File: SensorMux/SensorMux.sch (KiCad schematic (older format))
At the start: 0 parts

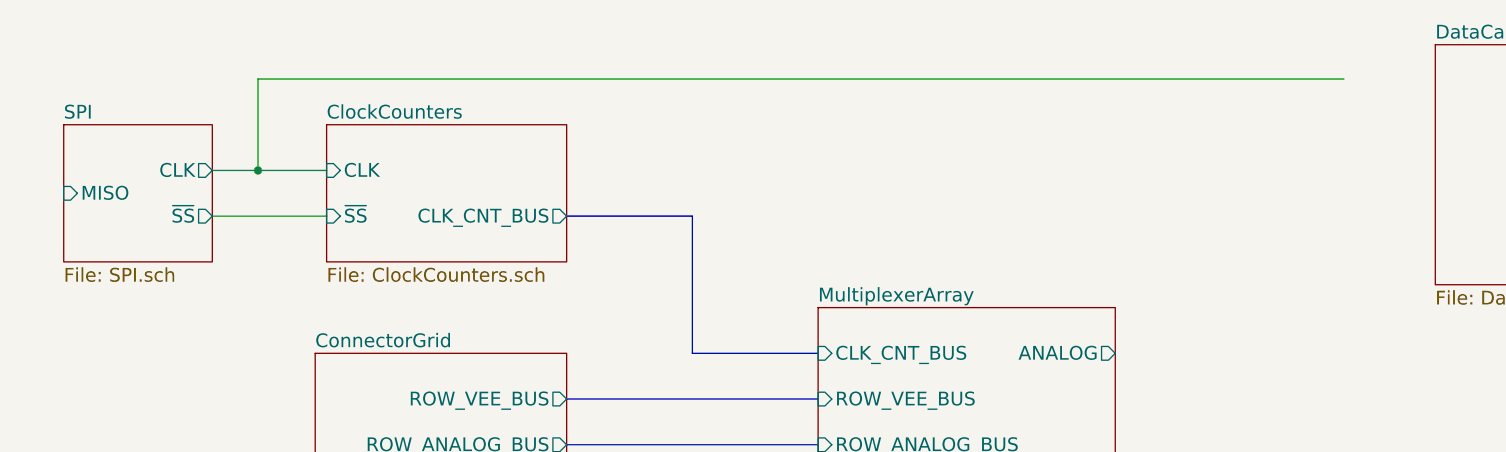
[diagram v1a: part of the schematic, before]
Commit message: Working on adding analog part with SPI adjustment so the computer can control the opamps without needing manual trimpots.
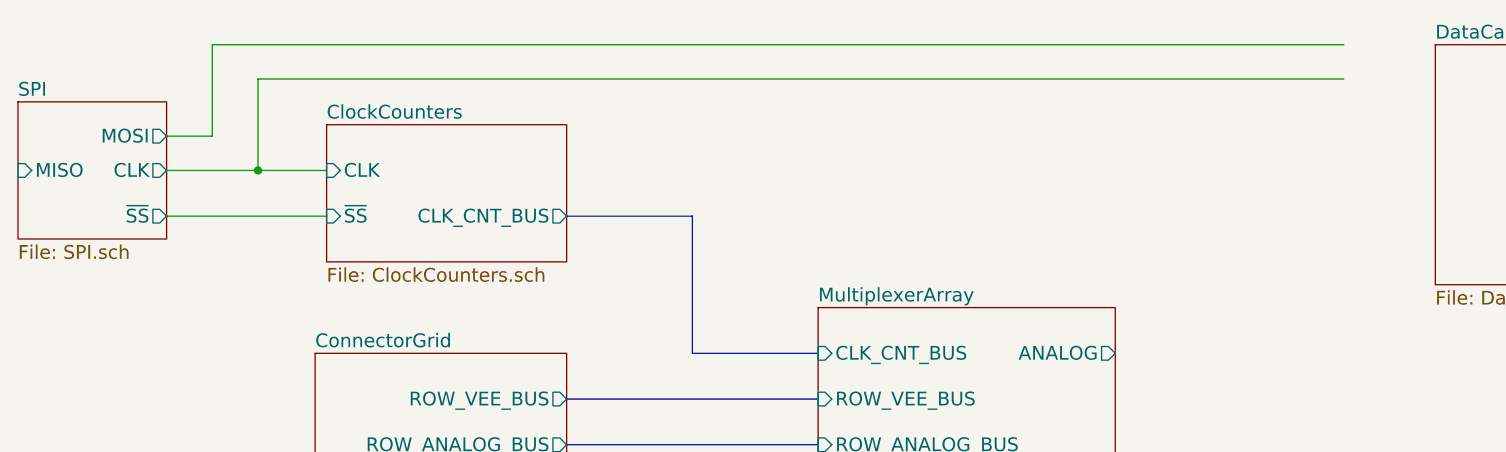
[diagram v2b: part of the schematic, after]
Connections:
- wire segments 4 -> 7
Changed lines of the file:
@@
 $EndSheet
 $Sheet
-S 1150 3500 650  600
+S 950  3400 650  600
 U 5A4A9682
 F0 "SPI" 60
 F1 "SPI.sch" 60
-F2 "MISO" I L 1150 3800 60
-F3 "~SS" O R 1800 3900 60
-F4 "CLK" O R 1800 3700 60
+F2 "MISO" I L 950 3700 60
+F3 "~SS" O R 1600 3900 60
+F4 "CLK" O R 1600 3700 60
+F5 "MOSI" O R 1600 3550 60
 $EndSheet
 $Sheet
@@
 $EndSheet
 Wire Wire Line
-	1800 3700 2300 3700
+	1600 3700 2300 3700
 Wire Wire Line
-	1800 3900 2300 3900
+	1600 3900 2300 3900
 Wire Bus Line
 	3350 3900 3900 3900
@@
 	2000 3300 6750 3300
 Connection ~ 2000 3700
+Wire Wire Line
+	1600 3550 1800 3550
+Wire Wire Line
+	1800 3550 1800 3150
+Wire Wire Line
+	1800 3150 6750 3150
 $EndSCHEMATC

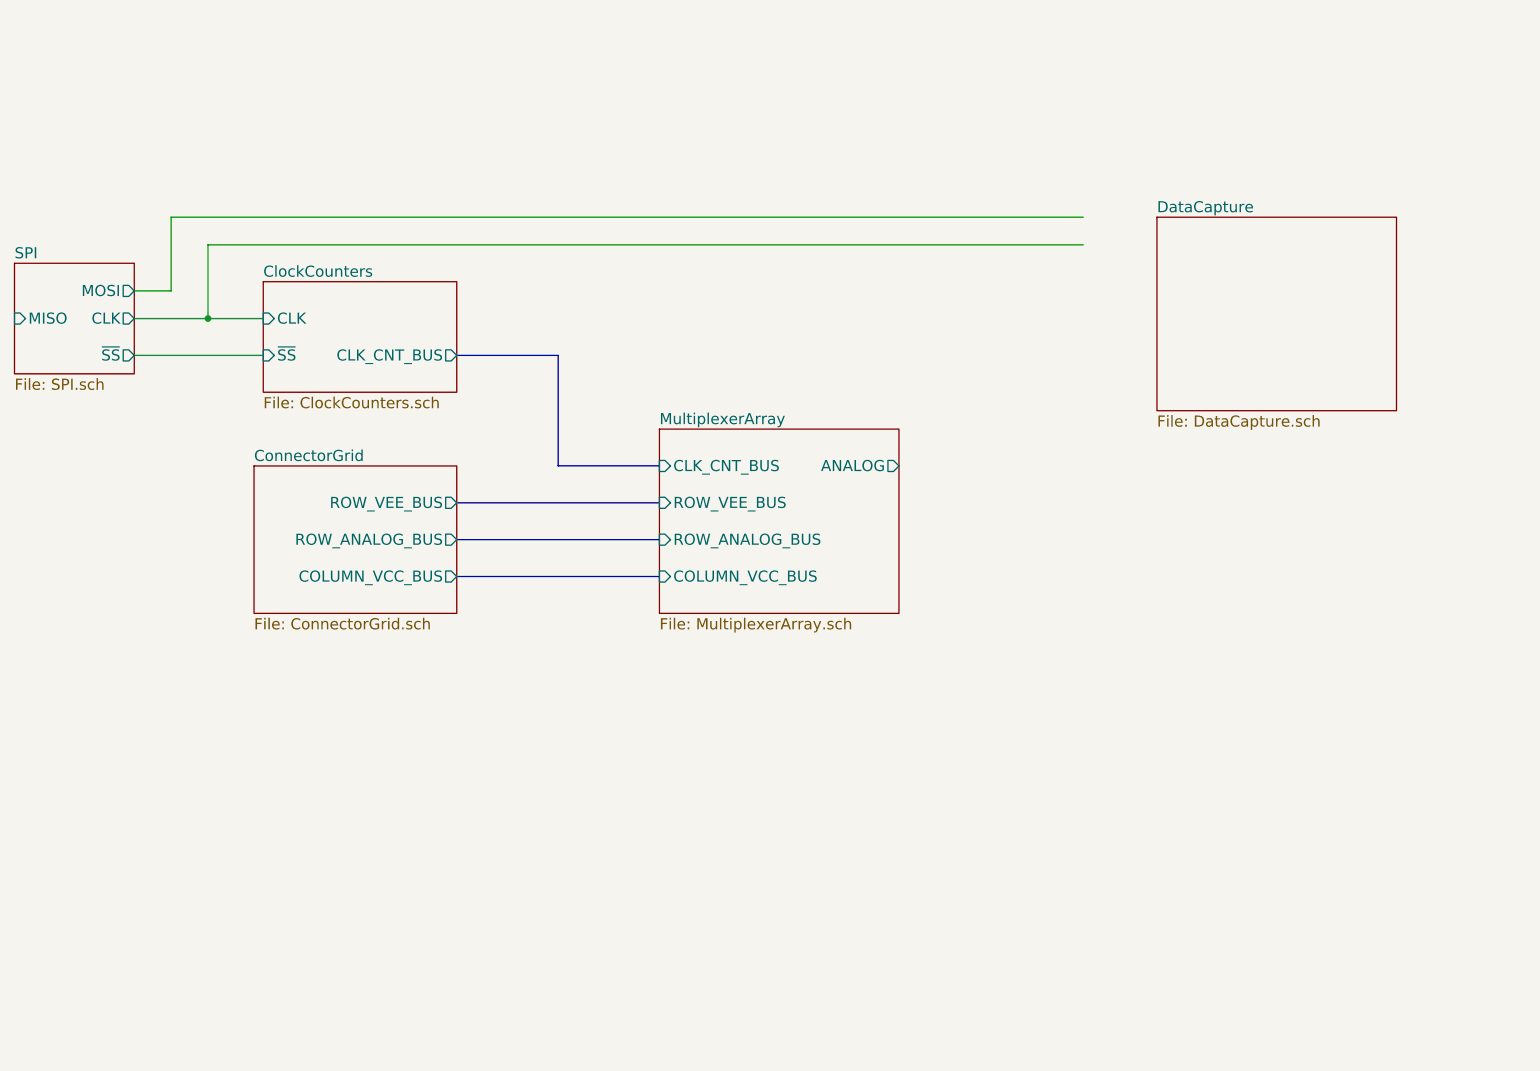
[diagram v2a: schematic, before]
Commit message: Working on the analog input.
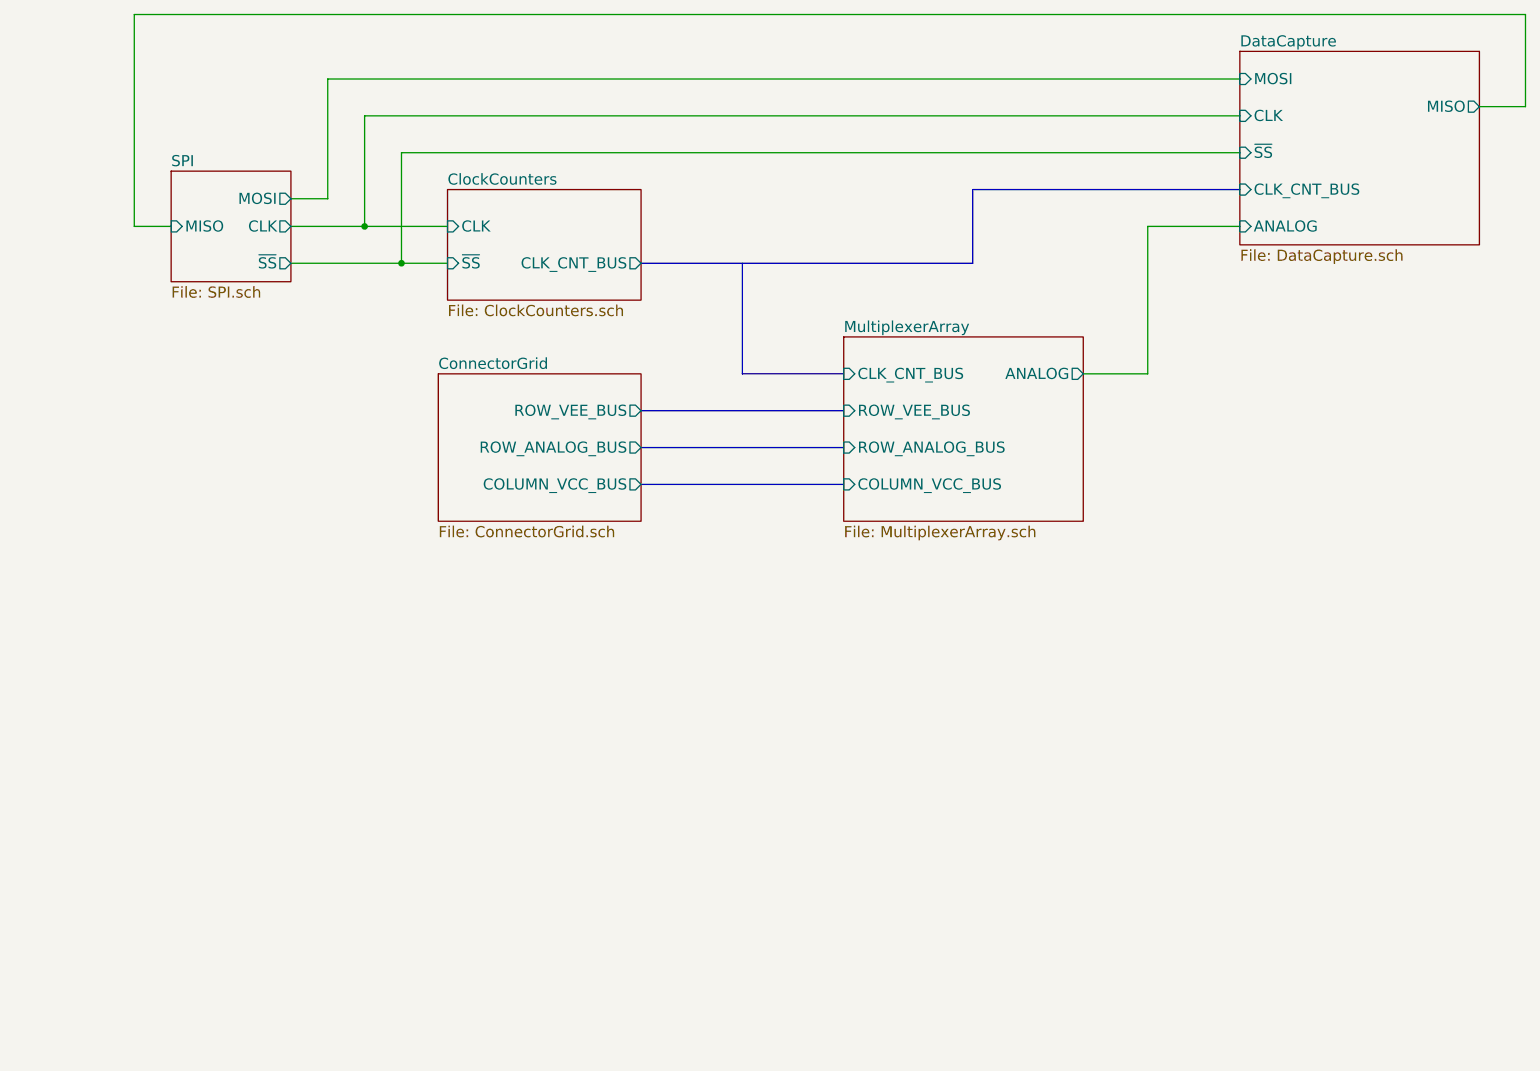
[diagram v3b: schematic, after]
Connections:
- wire segments 7 -> 17
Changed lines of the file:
@@
 $EndDescr
 $Sheet
-S 2300 3500 1050 600
+S 3300 3000 1050 600
 U 5A4A7F2E
 F0 "ClockCounters" 60
 F1 "ClockCounters.sch" 60
-F2 "~SS" I L 2300 3900 60
-F3 "CLK" I L 2300 3700 60
-F4 "CLK_CNT_BUS" O R 3350 3900 60
+F2 "~SS" I L 3300 3400 60
+F3 "CLK" I L 3300 3200 60
+F4 "CLK_CNT_BUS" O R 4350 3400 60
 $EndSheet
 $Sheet
-S 950  3400 650  600
+S 1800 2900 650  600
 U 5A4A9682
 F0 "SPI" 60
 F1 "SPI.sch" 60
-F2 "MISO" I L 950 3700 60
-F3 "~SS" O R 1600 3900 60
-F4 "CLK" O R 1600 3700 60
-F5 "MOSI" O R 1600 3550 60
+F2 "MISO" I L 1800 3200 60
+F3 "~SS" O R 2450 3400 60
+F4 "CLK" O R 2450 3200 60
+F5 "MOSI" O R 2450 3050 60
 $EndSheet
 $Sheet
-S 4450 4300 1300 1000
+S 5450 3800 1300 1000
 U 5A4ABEE0
 F0 "MultiplexerArray" 60
 F1 "MultiplexerArray.sch" 60
-F2 "CLK_CNT_BUS" I L 4450 4500 60
-F3 "ANALOG" O R 5750 4500 60
-F4 "COLUMN_VCC_BUS" I L 4450 5100 60
-F5 "ROW_ANALOG_BUS" I L 4450 4900 60
-F6 "ROW_VEE_BUS" I L 4450 4700 60
+F2 "CLK_CNT_BUS" I L 5450 4000 60
+F3 "ANALOG" O R 6750 4000 60
+F4 "COLUMN_VCC_BUS" I L 5450 4600 60
+F5 "ROW_ANALOG_BUS" I L 5450 4400 60
+F6 "ROW_VEE_BUS" I L 5450 4200 60
 $EndSheet
 $Sheet
-S 2250 4500 1100 800
+S 3250 4000 1100 800
 U 5A4B6DDC
 F0 "ConnectorGrid" 60
 F1 "ConnectorGrid.sch" 60
-F2 "ROW_VEE_BUS" O R 3350 4700 60
-F3 "ROW_ANALOG_BUS" O R 3350 4900 60
-F4 "COLUMN_VCC_BUS" O R 3350 5100 60
+F2 "ROW_VEE_BUS" O R 4350 4200 60
+F3 "ROW_ANALOG_BUS" O R 4350 4400 60
+F4 "COLUMN_VCC_BUS" O R 4350 4600 60
 $EndSheet
 $Sheet
-S 7150 3150 1300 1050
+S 7600 2250 1300 1050
 U 5A50AD3A
 F0 "DataCapture" 60
 F1 "DataCapture.sch" 60
+F2 "MISO" O R 8900 2550 60
+F3 "ANALOG" I L 7600 3200 60
+F4 "CLK" I L 7600 2600 60
+F5 "MOSI" I L 7600 2400 60
+F6 "CLK_CNT_BUS" I L 7600 3000 60
+F7 "~SS" I L 7600 2800 60
 $EndSheet
 Wire Wire Line
-	1600 3700 2300 3700
+	2450 3200 3300 3200
 Wire Wire Line
-	1600 3900 2300 3900
+	2450 3400 3300 3400
 Wire Bus Line
-	3350 3900 3900 3900
+	4350 3400 6150 3400
 Wire Bus Line
-	3900 3900 3900 4500
+	4900 3400 4900 4000
 Wire Bus Line
-	3900 4500 4450 4500
+	4900 4000 5450 4000
 Wire Bus Line
-	4450 4700 3350 4700
+	5450 4200 4350 4200
 Wire Bus Line
-	3350 4900 4450 4900
+	4350 4400 5450 4400
 Wire Bus Line
-	3350 5100 4450 5100
+	4350 4600 5450 4600
 Wire Wire Line
-	2000 3700 2000 3300
+	2850 3200 2850 2600
 Wire Wire Line
-	2000 3300 6750 3300
-Connection ~ 2000 3700
+	2850 2600 7600 2600
+Connection ~ 2850 3200
 Wire Wire Line
-	1600 3550 1800 3550
+	2450 3050 2650 3050
 Wire Wire Line
-	1800 3550 1800 3150
+	2650 3050 2650 2400
 Wire Wire Line
-	1800 3150 6750 3150
+	2650 2400 7600 2400
+Wire Wire Line
+	3050 3400 3050 2800
+Wire Wire Line
+	3050 2800 7600 2800
+Connection ~ 3050 3400
+Wire Bus Line
+	6150 3400 6150 3000
+Wire Bus Line
+	6150 3000 7600 3000
+Wire Wire Line
+	7600 3200 7100 3200
+Wire Wire Line
+	7100 3200 7100 4000
+Wire Wire Line
+	7100 4000 6750 4000
+Wire Wire Line
+	8900 2550 9150 2550
+Wire Wire Line
+	9150 2550 9150 2050
+Wire Wire Line
+	9150 2050 1600 2050
+Wire Wire Line
+	1600 2050 1600 3200
+Wire Wire Line
+	1600 3200 1800 3200
 $EndSCHEMATC

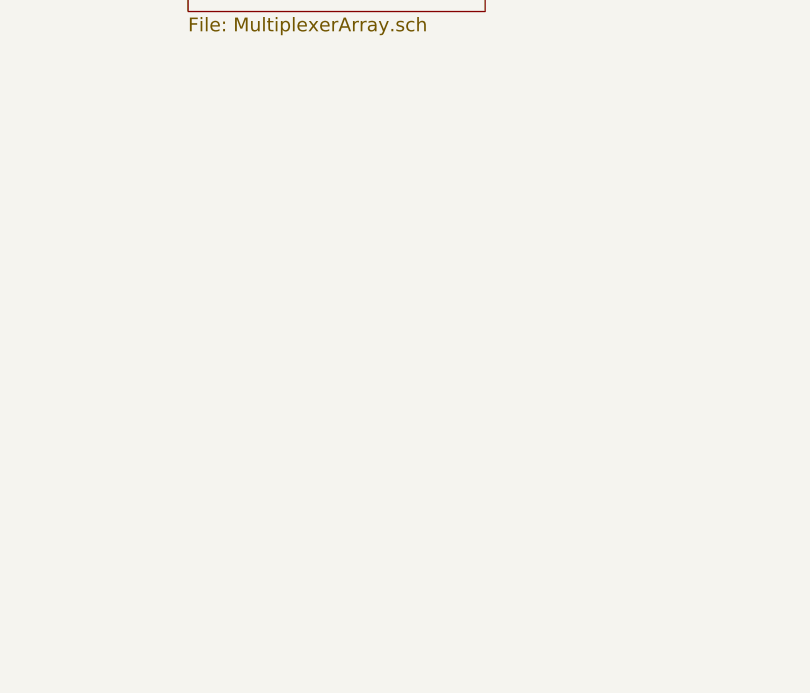
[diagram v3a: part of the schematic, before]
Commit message: Starting to prototype matrix connectors.
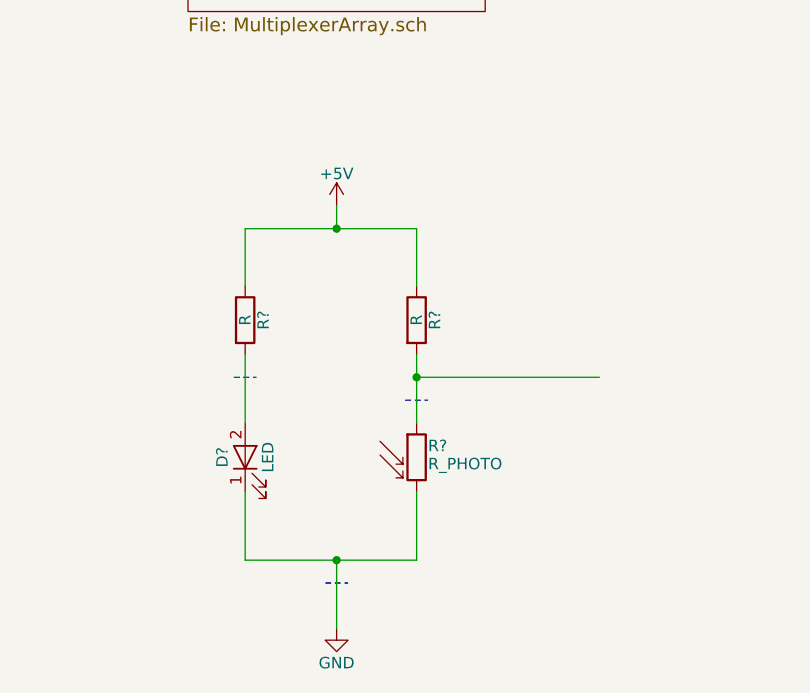
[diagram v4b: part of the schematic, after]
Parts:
- added D?: LED, symbol LED
- added R? (x2): R, symbol R
- added R?: R_PHOTO, symbol R_PHOTO
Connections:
- net labels added: +5V, GND
- wire segments 17 -> 28
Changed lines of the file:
@@
 Wire Wire Line
 	1600 3200 1800 3200
+$Comp
+L LED D?
+U 1 1 5A88D2DC
+P 5700 6750
+F 0 "D?" H 5700 6850 50  0000 C CNN
+F 1 "LED" H 5700 6650 50  0000 C CNN
+F 2 "" H 5700 6750 50  0001 C CNN
+F 3 "" H 5700 6750 50  0001 C CNN
+	1    5700 6750
+	0    -1   -1   0
+$EndComp
+$Comp
+L R R?
+U 1 1 5A88D398
+P 5700 6150
+F 0 "R?" V 5780 6150 50  0000 C CNN
+F 1 "R" V 5700 6150 50  0000 C CNN
+F 2 "" V 5630 6150 50  0001 C CNN
+F 3 "" H 5700 6150 50  0001 C CNN
+	1    5700 6150
+	1    0    0    -1
+$EndComp
+$Comp
+L GND #PWR?
+U 1 1 5A88D567
+P 6100 7500
+F 0 "#PWR?" H 6100 7250 50  0001 C CNN
+F 1 "GND" H 6100 7350 50  0000 C CNN
+F 2 "" H 6100 7500 50  0001 C CNN
+F 3 "" H 6100 7500 50  0001 C CNN
+	1    6100 7500
+	1    0    0    -1
+$EndComp
+$Comp
+L +5V #PWR?
+U 1 1 5A88D6F5
+P 6100 5650
+F 0 "#PWR?" H 6100 5500 50  0001 C CNN
+F 1 "+5V" H 6100 5790 50  0000 C CNN
+F 2 "" H 6100 5650 50  0001 C CNN
+F 3 "" H 6100 5650 50  0001 C CNN
+	1    6100 5650
+	1    0    0    -1
+$EndComp
+$Comp
+L R R?
+U 1 1 5A88D829
+P 6450 6150
+F 0 "R?" V 6530 6150 50  0000 C CNN
+F 1 "R" V 6450 6150 50  0000 C CNN
+F 2 "" V 6380 6150 50  0001 C CNN
+F 3 "" H 6450 6150 50  0001 C CNN
+	1    6450 6150
+	1    0    0    -1
+$EndComp
+$Comp
+L R_PHOTO R?
+U 1 1 5A88DD64
+P 6450 6750
+F 0 "R?" H 6500 6800 50  0000 L CNN
+F 1 "R_PHOTO" H 6500 6750 50  0000 L TNN
+F 2 "" V 6500 6500 50  0001 L CNN
+F 3 "" H 6450 6700 50  0001 C CNN
+	1    6450 6750
+	1    0    0    -1
+$EndComp
+Wire Wire Line
+	5700 6000 5700 5750
+Wire Wire Line
+	5700 5750 6450 5750
+Wire Wire Line
+	6100 5750 6100 5650
+Wire Wire Line
+	6450 5750 6450 6000
+Connection ~ 6100 5750
+Wire Wire Line
+	5700 6900 5700 7200
+Wire Wire Line
+	5700 7200 6450 7200
+Wire Wire Line
+	6100 7200 6100 7500
+Wire Wire Line
+	6450 7200 6450 6900
+Connection ~ 6100 7200
+Wire Wire Line
+	5700 6600 5700 6300
+Wire Wire Line
+	6450 6300 6450 6600
+Wire Wire Line
+	6450 6400 7250 6400
+Connection ~ 6450 6400
+Wire Notes Line
+	5650 6400 5750 6400
+Wire Notes Line
+	6400 6500 6500 6500
+Wire Notes Line
+	6050 7300 6150 7300
 $EndSCHEMATC
